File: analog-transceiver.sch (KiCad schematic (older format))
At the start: 166 parts, among them J1 BNC, J2 AF In, J3 AF Out, K1 G5Q-1, K2 G5Q-1, Q1 2N3904, Q10 2N3904, Q11 2N3904, Q12 2N3904, Q13 2N3904, Q14 2N3904, Q15 2N3906, Q16 BD140, Q17 2n3904, Q18 BF245A, Q19 2n2904, Q2 2N3904, Q21 BF245A, Q3 BF245A, Q4 2N3904, Q5 2N3904, Q6 2N3904, Q7 BD139, Q8 2N3904, Q9 2N3904, T1 2:8 Turns 43-material? iron p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, T2 iron powerder, Y1 10MHz, Y2 10MHz, Y3 10MHz, Y4 10MHz

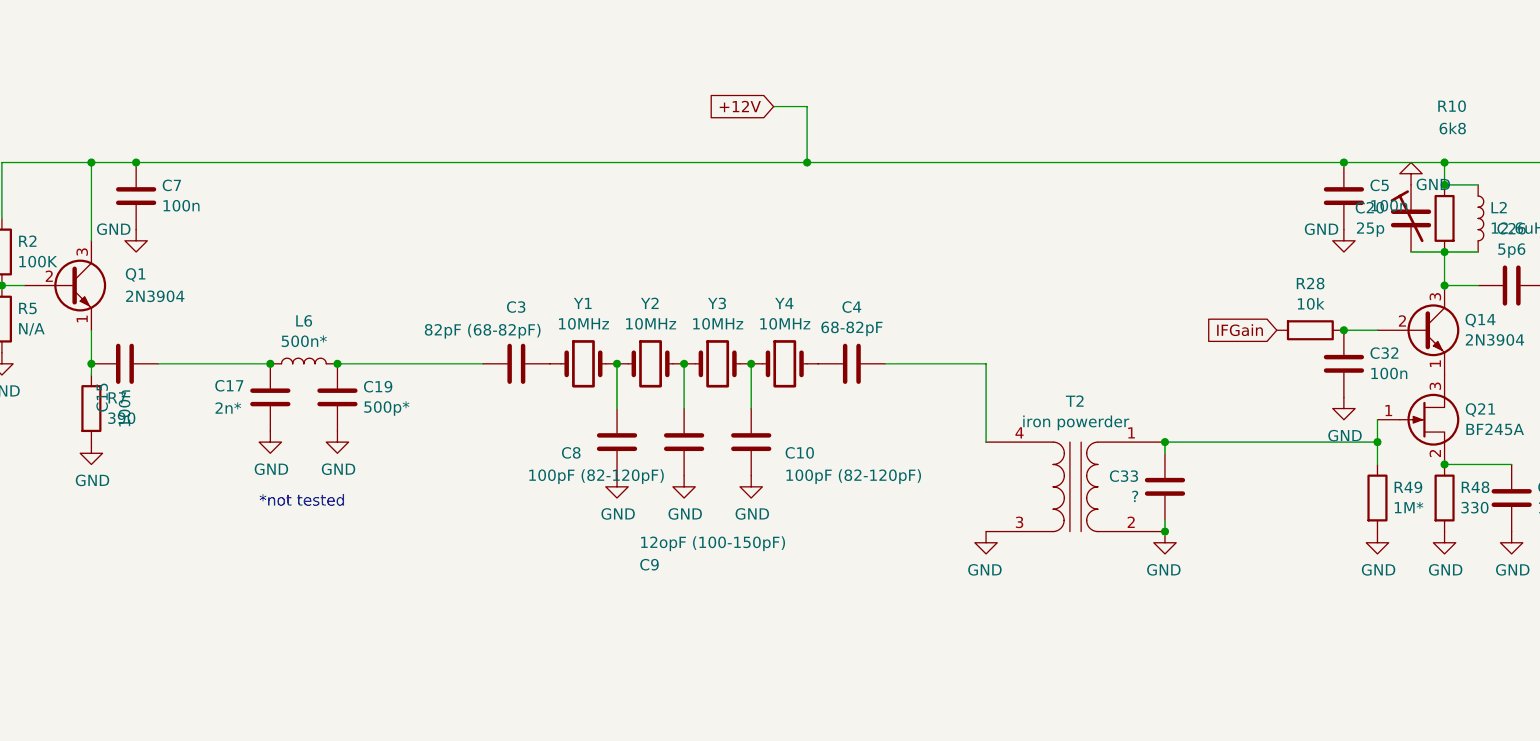
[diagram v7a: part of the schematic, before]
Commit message: Calculated and tested impedances for quartz filter - the values are correct now. Added buffer after quartz filter because jfet+bjt cascode changes its impedance with applied AGC voltage.
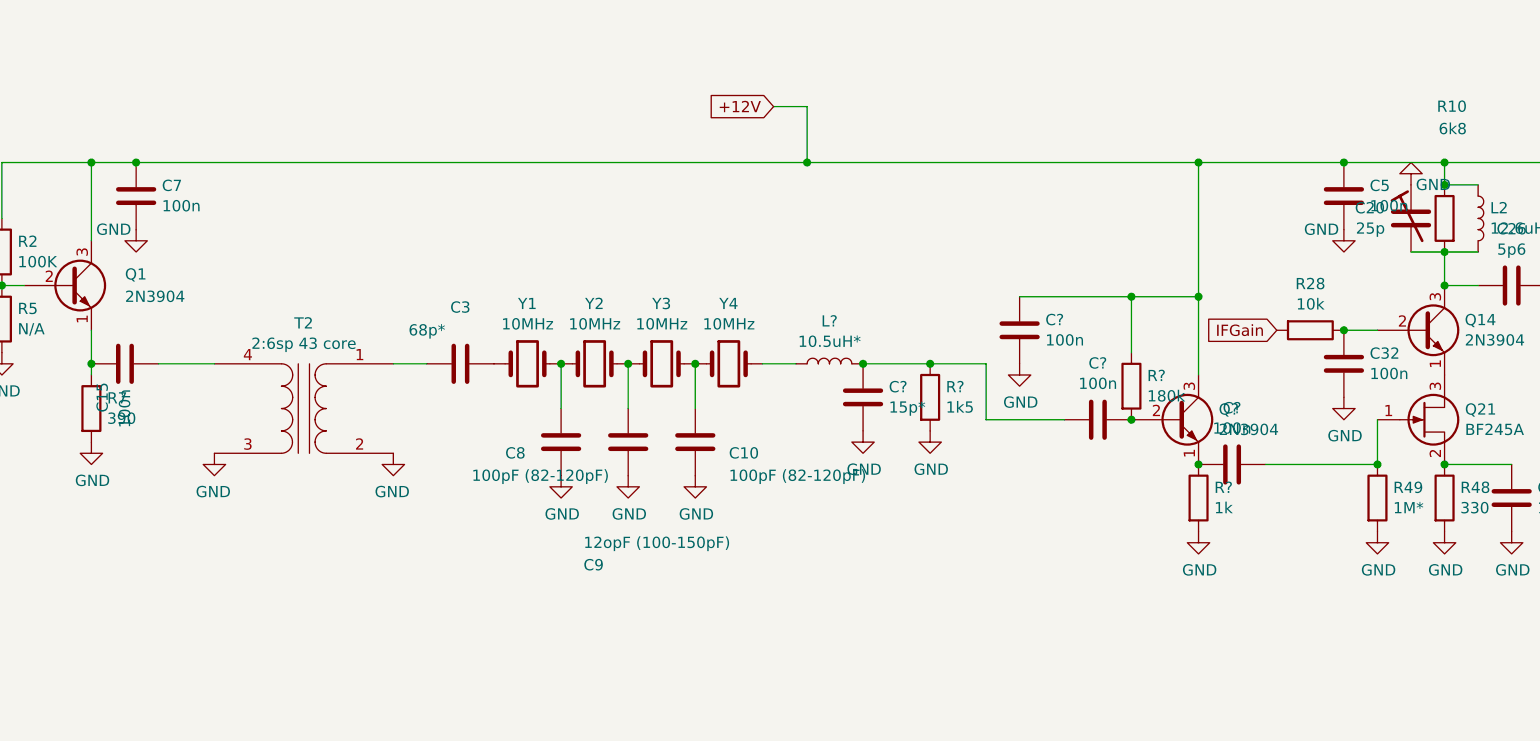
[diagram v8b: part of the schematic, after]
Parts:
- removed C17: 2n*, Capacitor_THT:C_Disc_D3.8mm_W2.6mm_P2.50mm, symbol Device:C
- removed C19: 500p*, Capacitor_THT:C_Disc_D3.8mm_W2.6mm_P2.50mm, symbol Device:C
- removed C33: ?, Capacitor_THT:C_Disc_D3.8mm_W2.6mm_P2.50mm, symbol Device:C
- removed C4: 68-82pF, Capacitor_THT:C_Disc_D3.8mm_W2.6mm_P2.50mm, symbol Device:C
- removed L6: 500n*, Inductor_THT:L_Toroid_Vertical_L10.0mm_W5.0mm_P5.08mm, symbol Device:L
- added C? (x3): 100n, symbol Device:C
- added C?: 15p*, symbol Device:C
- added L?: 10.5uH*, symbol Device:L
- added Q?: 2N3904, Package_TO_SOT_THT:TO-92_Inline, symbol Transistor_BJT:2N3904
- added R?: 1k, symbol Device:R
- added R?: 180k, symbol Device:R
- added R?: 1k5, symbol Device:R
- C3: value 82pF (68-82pF) -> 68p*
- T2: value iron powerder -> 2:6sp 43 core
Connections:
- net +12V: now also C?.1, Q?.3 (C), R?.1
- net GND: now also C?.2, C?.2, R?.2, R?.2
- net at C3.2: now also T2.1 (AA)
- net at T2.4 (SB): now also C15.2
- net at Y4.2: now also L?.1
- net at Q21.1 (G), R49.1: now also C?.1; no longer T2.1 (AA)
- new net: C?.2, Q?.1 (E), R?.1
- new net: C?.1, Q?.2 (B), R?.2
- new net: C?.1, C?.2, L?.2, R?.1
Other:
- note removed: "*not tested"
- moved on the sheet: C10, C3, C8, C9, T2, Y1, Y2, Y3, Y4
